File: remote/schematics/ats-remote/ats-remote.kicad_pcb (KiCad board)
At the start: 2 copper layers, 35.6 x 48.3 mm, 9 parts, among them J1 U1_1, J2 U1_2, J3 U2_2, J4 U2_1, J5 U3_1, J6 U3_2

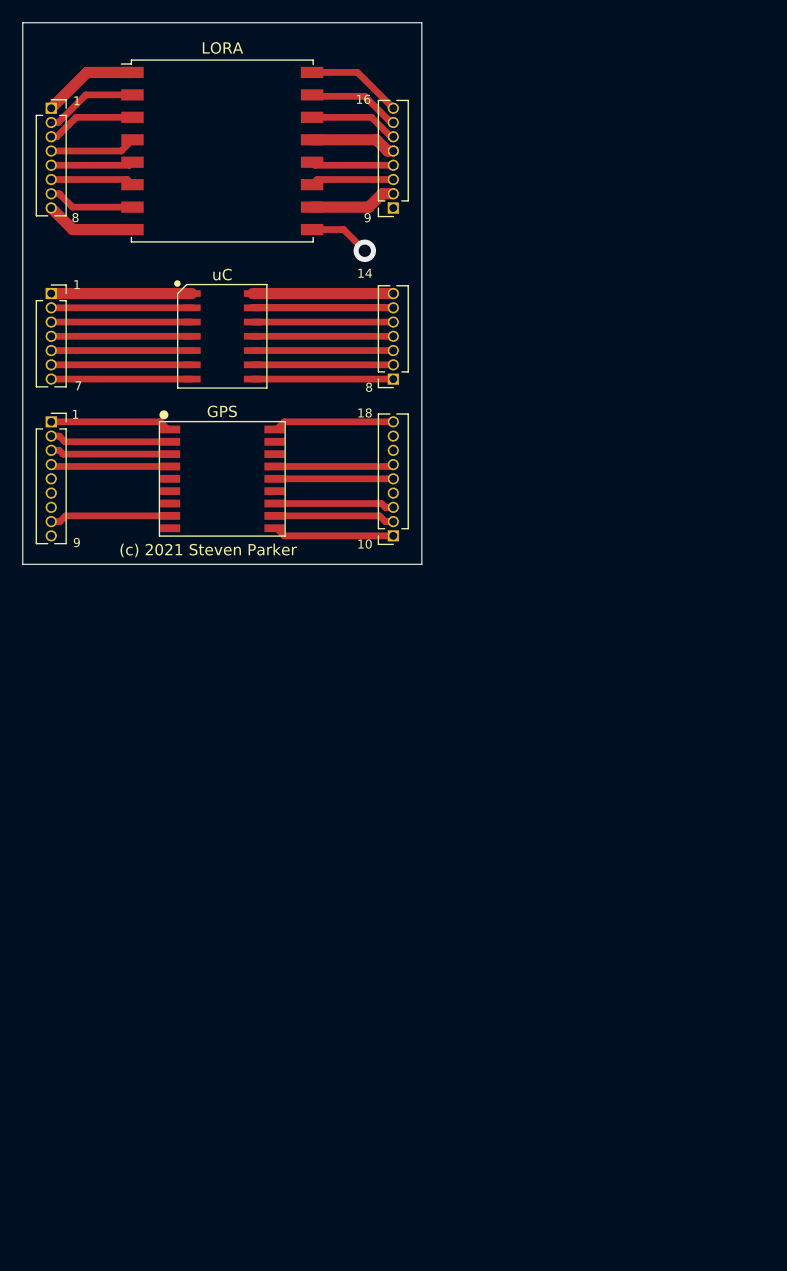
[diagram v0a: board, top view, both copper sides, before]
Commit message: add drill files
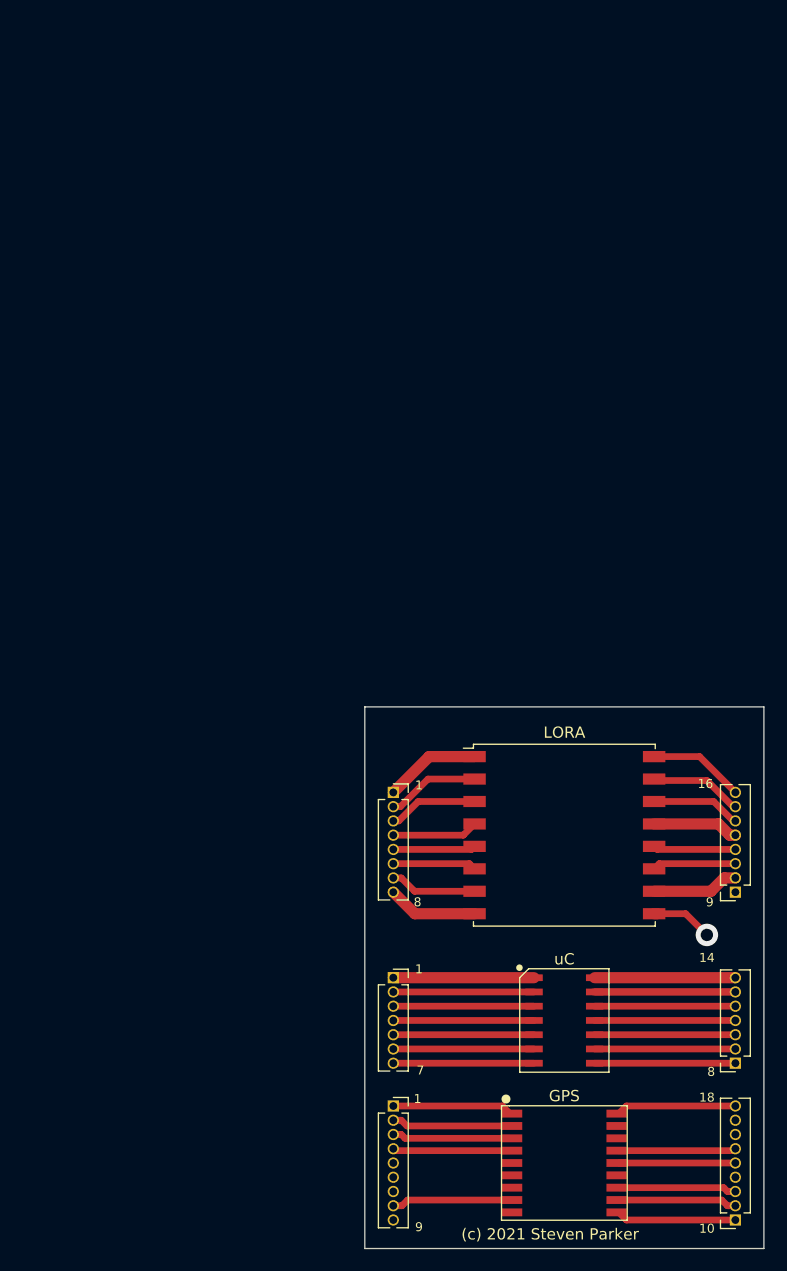
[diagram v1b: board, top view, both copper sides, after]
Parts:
- moved GPS 68.2 mm to (157.5, 115.6)
- moved J1 68.2 mm to (142.2, 82.5)
- moved J2 68.2 mm to (172.7, 91.4)
- moved J3 68.2 mm to (142.2, 99.1)
- moved J4 68.2 mm to (172.7, 106.7)
- moved J5 68.2 mm to (142.2, 110.5)
- moved J6 68.2 mm to (172.7, 120.7)
- moved uC 68.2 mm to (157.5, 102.9)
- moved LORA 68.2 mm to (157.5, 86.4)

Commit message: move remote schematic and pcb to v0.2.0 (#2)
v0.2.0

- 3.3v power and ground header
    - No OVP
    - No OCP
    - No polarity protection
    - Modules have their own decoupling caps
    - Modules have decoupling capacitors
- SPI header for LoRa module debug
- UART header for GPS module debug
- ICSP header for programming the PIC18
- LoRa module and SMD antenna
- GPS module and SMD antenna
- PIC18 controller
    - Controls SPI and UART
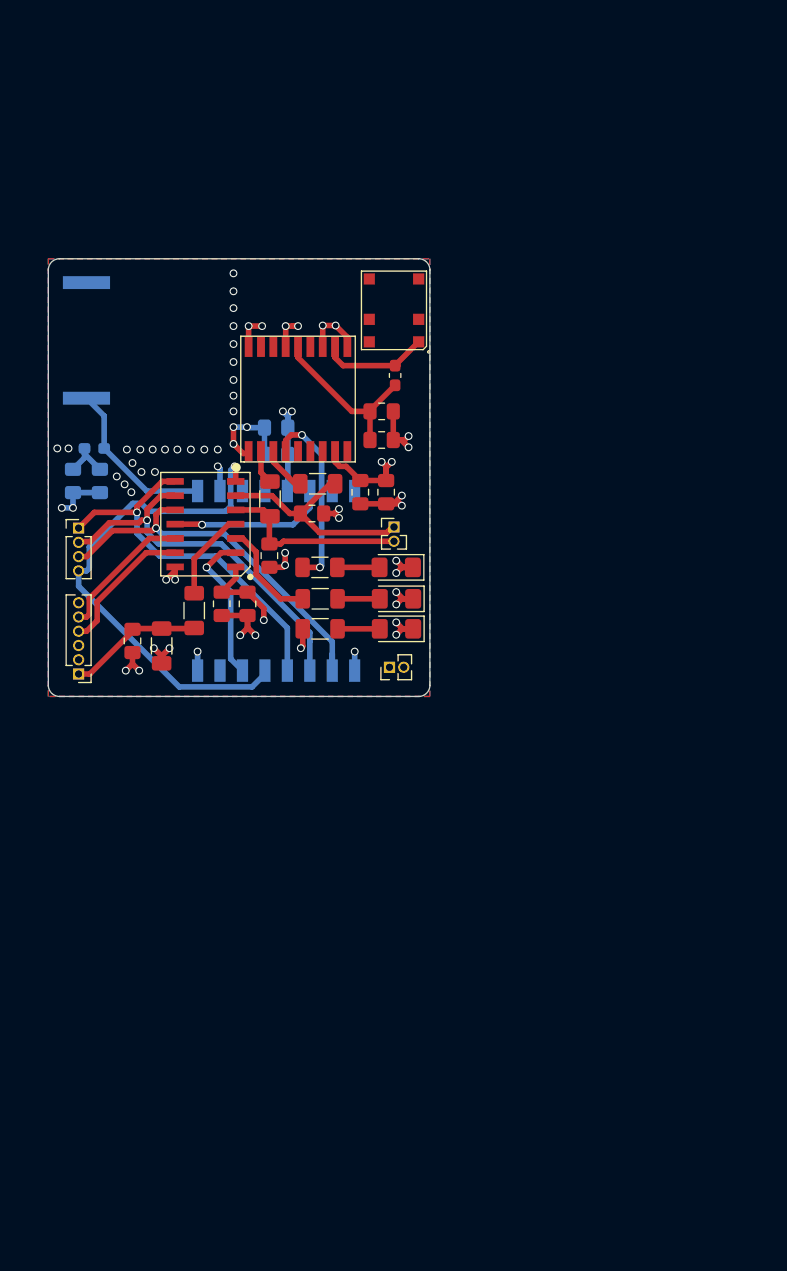
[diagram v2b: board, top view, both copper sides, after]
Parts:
- removed GPS: YIC71009EBGG, ats-remote:YIC71009EBGG-19STAMP
- removed J2: U1_2, Connector_PinSocket_1.27mm:PinSocket_1x08_P1.27mm_Vertical
- removed J3: U2_2, Connector_PinSocket_1.27mm:PinSocket_1x07_P1.27mm_Vertical
- removed J5: U3_1, Connector_PinSocket_1.27mm:PinSocket_1x09_P1.27mm_Vertical
- removed J6: U3_2, Connector_PinSocket_1.27mm:PinSocket_1x09_P1.27mm_Vertical
- removed LORA: RFM95W-915S2, RF_Module:HOPERF_RFM9XW_SMD
- removed uC: PIC18F06Q40, ats-remote:PIC18F06Q40-SOIC14
- added C1: 100n, Capacitor_SMD:C_0805_2012Metric_Pad1.18x1.45mm_HandSolder, F.Cu at (119.0, 69.0)
- added C10: 100n, Capacitor_SMD:C_0805_2012Metric_Pad1.18x1.45mm_HandSolder, B.Cu at (131.8, 52.5)
- added C11: 10n, Capacitor_SMD:C_0805_2012Metric_Pad1.18x1.45mm_HandSolder, F.Cu at (141.2, 48.6)
- added C12: 10n, Capacitor_SMD:C_0805_2012Metric_Pad1.18x1.45mm_HandSolder, B.Cu at (113.7, 54.8)
- added C13: 2.2u, Capacitor_SMD:C_0805_2012Metric_Pad1.18x1.45mm_HandSolder, B.Cu at (116.1, 54.8)
- added C2: 100p, Capacitor_SMD:C_0805_2012Metric_Pad1.18x1.45mm_HandSolder, F.Cu at (131.2, 61.5)
- added C3: 100p, Capacitor_SMD:C_0805_2012Metric_Pad1.18x1.45mm_HandSolder, F.Cu at (135.0, 57.7)
- added C4: 10n, Capacitor_SMD:C_0805_2012Metric_Pad1.18x1.45mm_HandSolder, F.Cu at (127.0, 65.8)
- added C5: 100n, Capacitor_SMD:C_0805_2012Metric_Pad1.18x1.45mm_HandSolder, F.Cu at (129.2, 65.8)
- added C6: 100p, Capacitor_SMD:C_0805_2012Metric_Pad1.18x1.45mm_HandSolder, F.Cu at (139.3, 55.8)
- added C7: 100p, Capacitor_SMD:C_0805_2012Metric_Pad1.18x1.45mm_HandSolder, F.Cu at (141.6, 55.8)
- added C8: 2.2u, Capacitor_SMD:C_0805_2012Metric_Pad1.18x1.45mm_HandSolder, F.Cu at (141.2, 51.1)
- added C9: 10n, Capacitor_SMD:C_0805_2012Metric_Pad1.18x1.45mm_HandSolder, B.Cu at (131.8, 50.0)
- added D1: LED_STATUS, Diode_SMD:D_1206_3216Metric_Pad1.42x1.75mm_HandSolder, F.Cu at (142.5, 65.3)
- added D2: LED_PWR, Diode_SMD:D_1206_3216Metric_Pad1.42x1.75mm_HandSolder, F.Cu at (142.5, 68.0)
- added D3: LED_PPS, Diode_SMD:D_1206_3216Metric_Pad1.42x1.75mm_HandSolder, F.Cu at (142.5, 62.5)
- added GPS ANT: GPS_ANT, ats-remote:GPS_ANT_SR4G008, F.Cu at (142.3, 39.6)
- added ICSP: ICSP, Connector_PinHeader_1.27mm:PinHeader_1x06_P1.27mm_Vertical, F.Cu at (114.2, 72.0)
- added L1: 33n, Inductor_SMD:L_0603_1608Metric_Pad1.05x0.95mm_HandSolder, F.Cu at (142.4, 45.4)
- added L2: 33n, Inductor_SMD:L_0603_1608Metric_Pad1.05x0.95mm_HandSolder, B.Cu at (115.6, 51.9)
- added LORA ANT: LORA_ANT, ats-remote:LORA_ANT_YIC71009EBGG, B.Cu at (119.5, 43.5)
- added PIC18: PIC18F06Q40, ats-remote:PIC18F06Q40-SOIC14, F.Cu at (125.5, 58.6)
- added R1: 2.2k, Resistor_SMD:R_1206_3216Metric_Pad1.30x1.75mm_HandSolder, F.Cu at (135.7, 65.3)
- added R2: 2.2k, Resistor_SMD:R_1206_3216Metric_Pad1.30x1.75mm_HandSolder, F.Cu at (135.7, 68.0)
- added R3: 10k, Resistor_SMD:R_1206_3216Metric_Pad1.30x1.75mm_HandSolder, F.Cu at (121.6, 69.5)
- added R4: 470, Resistor_SMD:R_1206_3216Metric_Pad1.30x1.75mm_HandSolder, F.Cu at (124.5, 66.3)
- added R5: 22, Resistor_SMD:R_1206_3216Metric_Pad1.30x1.75mm_HandSolder, F.Cu at (135.7, 62.5)
- added R6: 22, Resistor_SMD:R_1206_3216Metric_Pad1.30x1.75mm_HandSolder, F.Cu at (131.2, 56.4)
- added R7: 22, Resistor_SMD:R_1206_3216Metric_Pad1.30x1.75mm_HandSolder, F.Cu at (135.5, 55.0)
- added SPI: Conn_01x04_Male, Connector_PinHeader_1.27mm:PinHeader_1x04_P1.27mm_Vertical, F.Cu at (114.2, 59.0)
- added U1: RFM95W-915S2, RF_Module:HOPERF_RFM9XW_SMD, B.Cu at (131.8, 63.7)
- added YIC: YIC71009EBGG, ats-remote:YIC71009EBGG-19STAMP, F.Cu at (133.8, 47.5)
- J1: value U1_1 -> PWR; footprint Connector_PinSocket_1.27mm:PinSocket_1x08_P1.27mm_Vertical -> Connector_PinHeader_1.27mm:PinHeader_1x02_P1.27mm_Vertical
- J4: value U2_1 -> Conn_01x02_Male; footprint Connector_PinSocket_1.27mm:PinSocket_1x07_P1.27mm_Vertical -> Connector_PinHeader_1.27mm:PinHeader_1x02_P1.27mm_Vertical
- moved J4 56.6 mm to (142.3, 58.9), turned to 0 degrees
- moved J1 11.2 mm to (141.9, 71.4), turned to 90 degrees
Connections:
- J1 pad 1: LORA_GND_1 -> +3V3
- J1 pad 2: LORA_MISO -> GND
- J4 pad 1: PIC_RC2 -> YIC_RXD
- J4 pad 2: PIC_RC1 -> YIC_TXD
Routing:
- net GND: track 0.00 -> 69.2 mm, vias 0 -> 59
- net LORA_NSS: track 7.35 -> 45.5 mm, vias 0 -> 1
- net +3V3: track 0.00 -> 32.1 mm, vias 0 -> 8
- net LORA_MISO: track 8.26 -> 35.8 mm, vias 0 -> 1
- net LORA_MOSI: track 7.96 -> 34.4 mm, vias 0 -> 1
- net LORA_SCK: track 7.65 -> 33.8 mm, vias 0 -> 1
- net PIC_RA0: track 25.2 -> 0.00 mm
- net Net-(R5-Pad1): track 0.00 -> 17.0 mm, vias 0 -> 2
- net Net-(C11-Pad2): track 0.00 -> 15.4 mm
- net Net-(AE2-Pad1): track 0.00 -> 15.0 mm
- net PIC_VSS: track 12.5 -> 0.00 mm
- net PIC_VDD: track 12.5 -> 0.00 mm
- net PIC_RC5: track 12.5 -> 0.00 mm
- net PIC_RC4: track 12.5 -> 0.00 mm
- net PIC_RC3: track 12.5 -> 0.00 mm
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- added copper zone on 3v3.Cu, net +3V3
- added copper zone on B.Cu, net GND
- added copper zone on F.Cu, net GND
- added copper zone on GND.Cu, net GND
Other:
- board size 35.6 x 48.3 mm -> 34 x 39 mm
- copper layers 2 -> 4
- net class Default: via_dia 0.8 -> 0.5; via_drill 0.4 -> 0.3
- rule trace_min: 0.6 -> 0.3
- board text removed: "(c) 2021 Steven Parker"
- board text removed: "1"
- board text removed: "10"
- board text removed: "14"
- board text removed: "16"
- board text removed: "18"
- board text removed: "7"
- board text removed: "8"
- board text removed: "9"

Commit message: v0.2.1 (#3)
* add footprints for gps and lora antennas; start work on new board

* update schematic and pcb to v0.2.0

* Update README.md

* remove gerber files

* update schematic and pcb

* add silk screen

* update silk screen

* fix lora nss via and gps ant grounds
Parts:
- removed GPS ANT: GPS_ANT, ats-remote:GPS_ANT_SR4G008
- added AE1: GPS_ANT, ats-remote:GPS_ANT_SR4G008, F.Cu at (140.5, 38.3)
- added C14: 10n, Capacitor_SMD:C_0805_2012Metric_Pad1.18x1.45mm_HandSolder, F.Cu at (140.2, 43.6)
- added L3: 33n, Inductor_SMD:L_0603_1608Metric_Pad1.05x0.95mm_HandSolder, F.Cu at (142.1, 46.9)
- added L4: 33n, Inductor_SMD:L_0603_1608Metric_Pad1.05x0.95mm_HandSolder, F.Cu at (142.1, 43.4)
- AE2: renamed from LORA ANT
- C13, C8: value 2.2u -> 2u2
- C6: value 100p -> 2u2
- C7: value 100p -> 10n
- J3: renamed from SPI; value Conn_01x04_Male -> SPI
- J4: value Conn_01x02_Male -> UART
- R1, R2: value 2.2k -> 2k2
- R5: value 22 -> 2k2
- moved J3 3.90 mm to (114.2, 62.9), turned to 180 degrees
- moved L1 3.06 mm to (140.0, 47.3)
- moved C11 2.77 mm to (142.4, 51.1), turned to 90 degrees
- moved D1 1.20 mm to (141.3, 65.3)
- moved D2 1.20 mm to (141.3, 68.0)
- moved D3 1.20 mm to (141.3, 62.5)
- moved C8 1.00 mm to (140.2, 51.1), turned to 90 degrees
- renumbered ICSP to J2, PIC18 to U2, YIC to U3
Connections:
- J3 pad 1: LORA_SCK -> LORA_NSS
- J3 pad 2: LORA_MOSI -> LORA_MISO
- J3 pad 3: LORA_MISO -> LORA_MOSI
- J3 pad 4: LORA_NSS -> LORA_SCK
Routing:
- net +3V3: track 32.1 -> 109.8 mm
- net GND: track 69.2 -> 77.3 mm, vias 59 -> 83
- net Net-(AE1-Pad2): track 0.00 -> 4.19 mm
- net LORA_NSS: track 45.5 -> 47.5 mm
- net Net-(C11-Pad2): track 15.4 -> 13.4 mm
- net Net-(D2-Pad2): track 3.76 -> 2.56 mm
- net Net-(D1-Pad2): track 3.76 -> 2.56 mm
- net Net-(D3-Pad2): track 3.76 -> 2.56 mm
- net Net-(C14-Pad2): track 10.1 -> 9.14 mm
- added copper zone on 3v3.Cu, net GND
- removed copper zone on 3v3.Cu, net +3V3
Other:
- net class 50ohm @ JLCPCB type JLC7628 added: clearance 0.6, trace_width 0.29337, via_dia 0.5, via_drill 0.3
- rule trace_min: 0.3 -> 0.2
- board text added: "3v3"
- board text added: "CLK"
- board text added: "DAT"
- board text added: "GND"
- board text added: "GPS ANT"
- board text added: "LORA ANT"
- board text added: "MCLR"
- board text added: "MISO"
- board text added: "MOSI"
- board text added: "PIC18F06"
- board text added: "RX"
- board text added: "SCK"
- board text added: "SS"
- board text added: "TX"
- board text added: "YIC71009EBGG"

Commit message: update silkscreen to include copyright
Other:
- board text added: "(c) 2021 Steven Parker Rev: v0.2.1"
- board text added: "RFM95W"
